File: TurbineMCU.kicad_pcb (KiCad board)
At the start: 4 copper layers, 53.7 x 54.7 mm, 44 parts, among them IC1 MSPM0G3507SPMR, IC2 TPS73533DRVT, J1 Conn_01x02_Socket, J10 Conn_01x03_Socket, J13 Conn_01x03_Socket, J14 Conn_01x03_Socket, J15 Conn_01x08_Pin, J2 Conn_01x02_Socket, J3 Conn_01x04_Socket, J5 Conn_01x03_Socket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

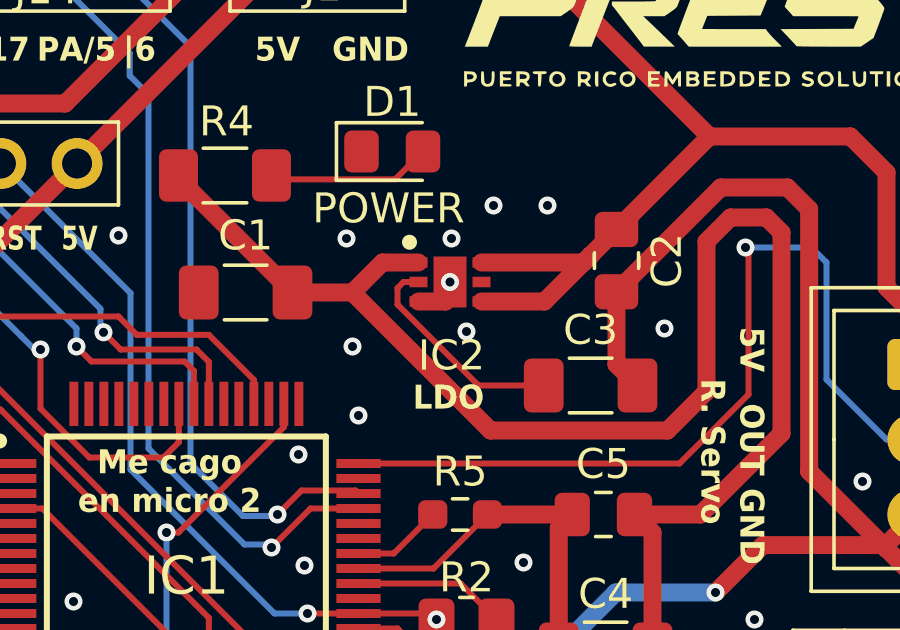
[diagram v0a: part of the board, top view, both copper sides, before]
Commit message: Fixed library and step model path
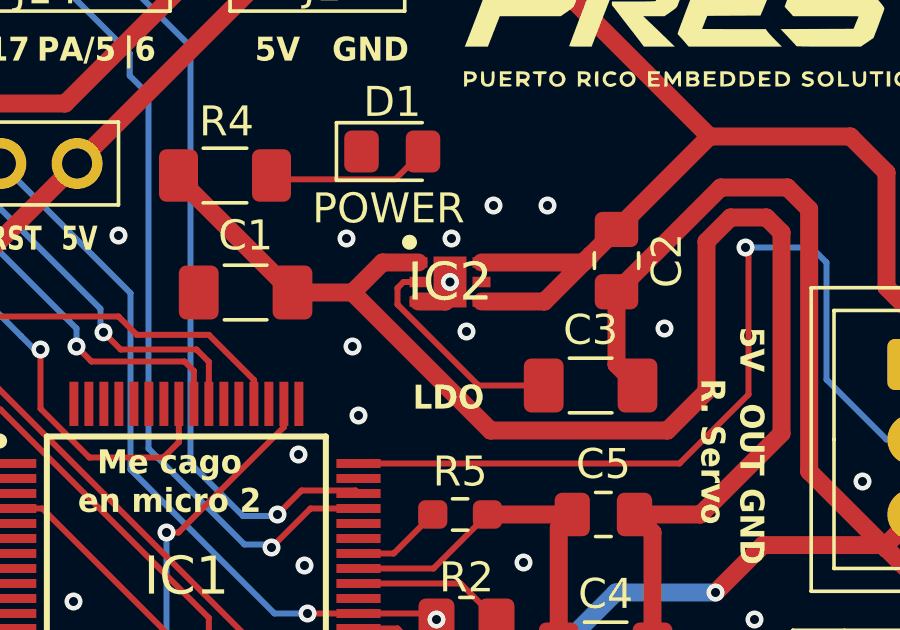
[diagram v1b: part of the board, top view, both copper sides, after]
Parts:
- IC1: footprint MSPM03507:QFP50P1200X1200X160-64N -> MSPM0SPMR:QFP50P1200X1200X160-64N
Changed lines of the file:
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@@
 		)
 	)
-	(footprint "MSPM03507:QFP50P1200X1200X160-64N"
+	(footprint "MSPM0SPMR:QFP50P1200X1200X160-64N"
 		(layer "F.Cu")
 		(at 171.262 91.85)
@@
 			)
 		)
-		(property "Datasheet" "https://www.ti.com/lit/ds/symlink/mspm0g3505.pdf?ts=1706855132968"
+		(property "Datasheet" ""
 			(at 0 0 0)
 			(layer "F.Fab")
@@
 			)
 		)
-		(property "Description" "ARM Microcontrollers - MCU 80MHz Arm M0+ MCU, 128KB Flash, 32KB SRAM, 212bit 4Msps ADC, DAC, 3COMP, 3op-amp, CAN-FD, MATHACL 64-LQFP -40 to 125"
+		(property "Description" ""
 			(at 0 0 0)
 			(layer "F.Fab")
@@
 		)
 		(embedded_fonts no)
-		(model "/Users/hiramraul11gmail.com/Downloads/LQFP64 v1.step"
+		(model "${KIPRJMOD}/mylib/LQFP64 v1.step"
 			(offset
 				(xyz 0 0 0)
@@
 		)
 		(embedded_fonts no)
-		(model "/Users/hiramraul11gmail.com/Downloads/kf128-screw-terminal-2-54-mm-pitch-1.snapshot.2/KF128 2.54mm/KF128-2.54-3P.step"
+		(model "${KIPRJMOD}/mylib/kf128-screw-terminal-2-54-mm-pitch-1.snapshot.2/KF128 2.54mm/KF128-2.54-3P.step"
 			(offset
 				(xyz 2.5 0 0)
@@
 		(tags "Integrated Circuit")
 		(property "Reference" "IC2"
-			(at 0.05 2.45 0)
+			(at 0 0 0)
 			(layer "F.SilkS")
 			(effects
 				(font
-					(size 1 1)
-					(thickness 0.15)
+					(size 1.27 1.27)
+					(thickness 0.254)
 				)
 			)
@@
 			)
 		)
-		(property "Datasheet" "http://www.ti.com/lit/ds/symlink/tps735.pdf"
+		(property "Datasheet" ""
 			(at 0 0 0)
 			(layer "F.Fab")
@@
 			)
 		)
-		(property "Description" "500mA 3.3V Low IQ/Noise LDO Reg. WSON6EP TPS73533DRVT, Low Dropout Voltage Regulator, 500mA, 1  4.3 V +/-1%, 6-Pin SON"
+		(property "Description" ""
 			(at 0 0 0)
 			(layer "F.Fab")
@@
 		)
 		(fp_text user "${REFERENCE}"
-			(at 0.15 0.15 0)
+			(at 0 0 0)
 			(layer "F.Fab")
 			(effects
@@
 		)
 		(embedded_fonts no)
-		(model "/Users/hiramraul11gmail.com/Downloads/WSON-6_2x2.step"
+		(model "${KIPRJMOD}/mylib/WSON-6_2x2.step"
 			(offset
 				(xyz 0 0 0)
@@
 		)
 		(embedded_fonts no)
-		(model "/Users/hiramraul11gmail.com/Downloads/kf128-screw-terminal-2-54-mm-pitch-1.snapshot.2/KF128 2.54mm/KF128-2.54-3P.step"
+		(model "${KIPRJMOD}/mylib/kf128-screw-terminal-2-54-mm-pitch-1.snapshot.2/KF128 2.54mm/KF128-2.54-3P.step"
 			(offset
 				(xyz 2.5 0 0)
@@
 		)
 		(embedded_fonts no)
-		(model "/Users/hiramraul11gmail.com/Downloads/kf128-screw-terminal-2-54-mm-pitch-1.snapshot.2/KF128 2.54mm/KF128-2.54-2P.step"
+		(model "${KIPRJMOD}/mylib/kf128-screw-terminal-2-54-mm-pitch-1.snapshot.2/KF128 2.54mm/KF128-2.54-2P.step"
 			(offset
 				(xyz 1.2 0 0)
@@
 		)
 		(embedded_fonts no)
-		(model "/Users/hiramraul11gmail.com/Downloads/kf128-screw-terminal-2-54-mm-pitch-1.snapshot.2/KF128 2.54mm/KF128-2.54-3P.step"
+		(model "${KIPRJMOD}/mylib/kf128-screw-terminal-2-54-mm-pitch-1.snapshot.2/KF128 2.54mm/KF128-2.54-3P.step"
 			(offset
 				(xyz 2.5 0 0)
@@
 		)
 		(embedded_fonts no)
-		(model "/Users/hiramraul11gmail.com/Downloads/kf128-screw-terminal-2-54-mm-pitch-1.snapshot.2/KF128 2.54mm/KF128-2.54-2P.step"
+		(model "${KIPRJMOD}/mylib/kf128-screw-terminal-2-54-mm-pitch-1.snapshot.2/KF128 2.54mm/KF128-2.54-2P.step"
 			(offset
 				(xyz 1.2 0 0)
